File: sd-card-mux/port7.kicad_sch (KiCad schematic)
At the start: 10 parts, among them J201 47309-2285, U201 74LVC1G3157, U202 74LVC1G3157, U203 74LVC1G3157, U204 74LVC1G3157, U205 74LVC1G3157, U206 74LVC1G3157

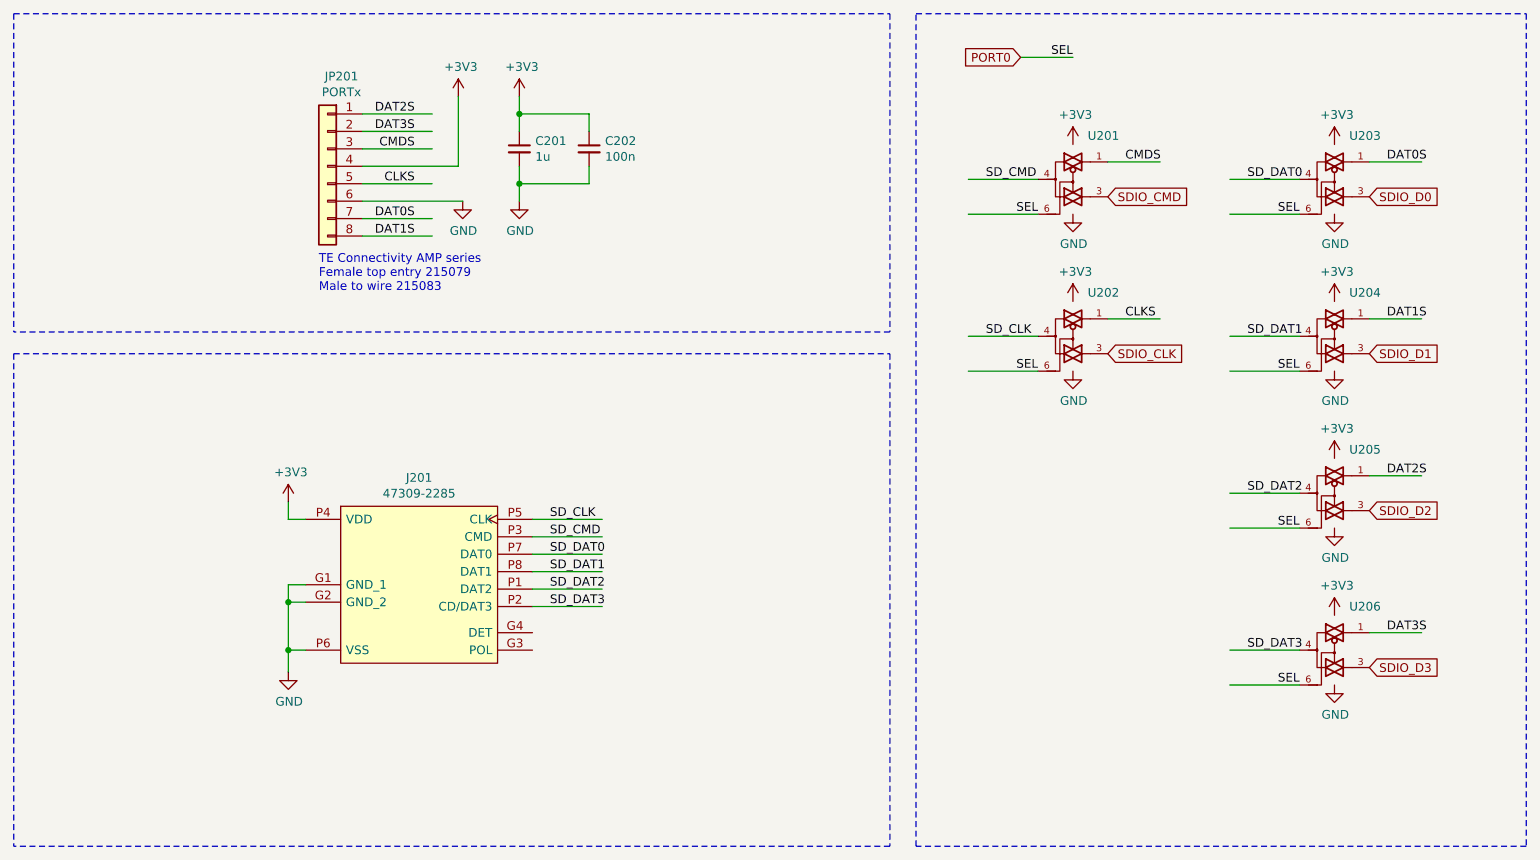
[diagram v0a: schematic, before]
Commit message: Added MCP23008 alternative
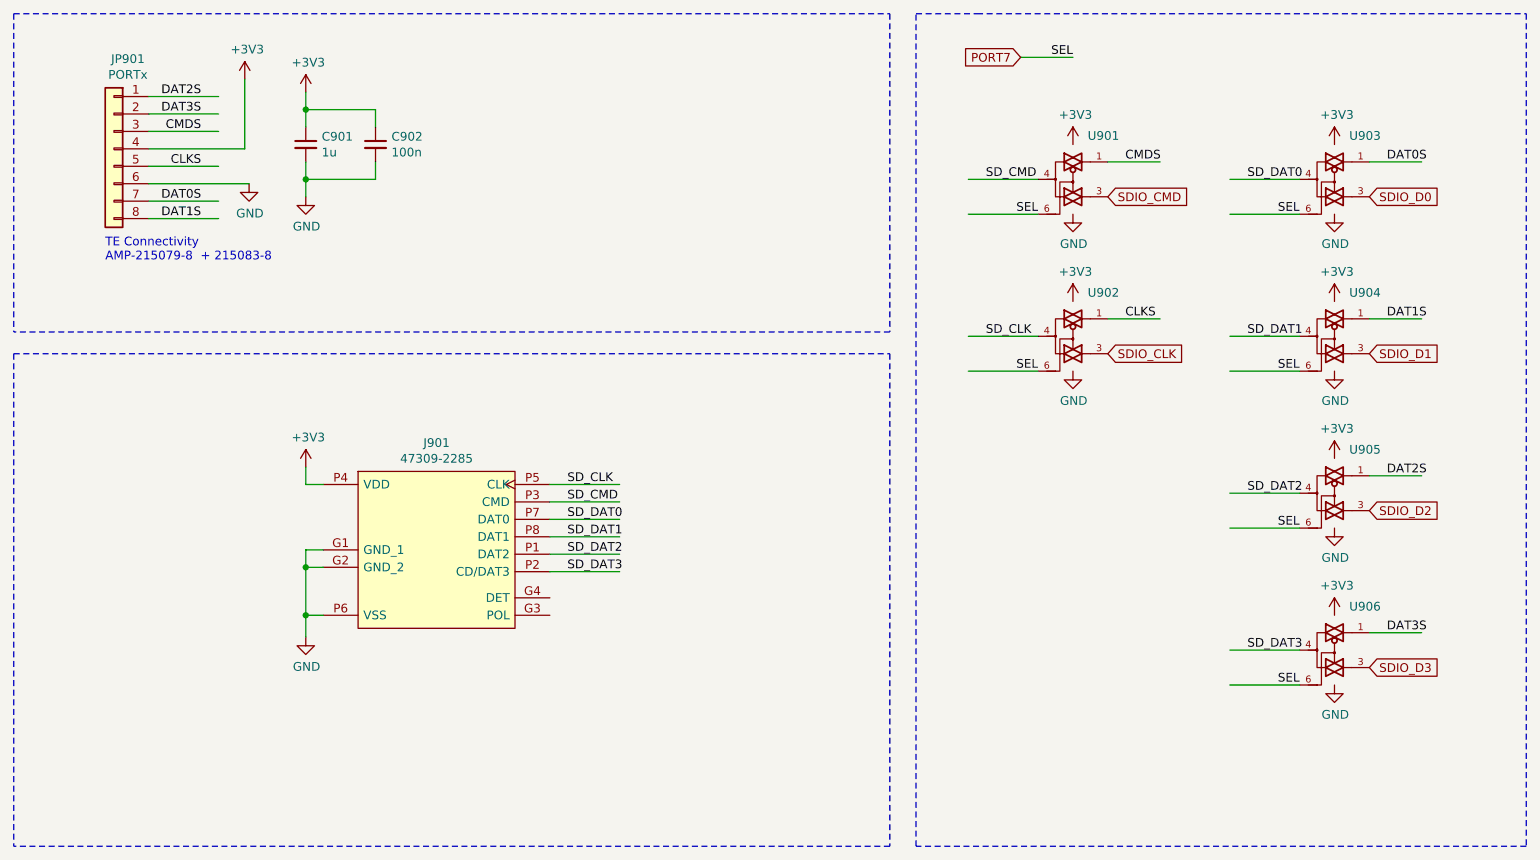
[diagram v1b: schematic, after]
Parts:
- removed C201: 1u, Capacitor_SMD:C_0402_1005Metric, symbol Device:C_Small
- removed C202: 100n, Capacitor_SMD:C_0402_1005Metric, symbol Device:C_Small
- removed J201: 47309-2285, footprints:47309-2285, symbol 47309-2285:47309-2285
- removed JP201: PORTx, Connector_JST:JST_PH_S8B-PH-K_1x08_P2.00mm_Horizontal, symbol Connector_Generic:Conn_01x08
- removed U201, U202, U203, U204, U205, U206: 74LVC1G3157, Package_TO_SOT_SMD:SOT-363_SC-70-6, symbol 74LVC1G3157:74LVC1G3157
- added C901: 1u, Capacitor_SMD:C_0402_1005Metric, symbol Device:C_Small
- added C902: 100n, Capacitor_SMD:C_0402_1005Metric, symbol Device:C_Small
- added J901: 47309-2285, footprints:47309-2285, symbol 47309-2285:47309-2285
- added JP901: PORTx, Connector_JST:JST_PH_S8B-PH-K_1x08_P2.00mm_Horizontal, symbol Connector_Generic:Conn_01x08
- added U901, U902, U903, U904, U905, U906: 74LVC1G3157, Package_TO_SOT_SMD:SOT-363_SC-70-6, symbol 74LVC1G3157:74LVC1G3157
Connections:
- net +3V3: now also C901.1, C902.1, J901.P4 (VDD), JP901.4 (Pin_4), U901.5 (VCC), U902.5 (VCC), U903.5 (VCC), U904.5 (VCC), U905.5 (VCC), U906.5 (VCC)
- net CLKS: now also JP901.5 (Pin_5), U902.1
- net CMDS: now also JP901.3 (Pin_3), U901.1
- net DAT0S: now also JP901.7 (Pin_7), U903.1
- net DAT1S: now also JP901.8 (Pin_8), U904.1
- net DAT2S: now also JP901.1 (Pin_1), U905.1
- net DAT3S: now also JP901.2 (Pin_2), U906.1
- net GND: now also C901.2, C902.2, J901.G1 (GND_1), J901.G2 (GND_2), J901.P6 (VSS), JP901.6 (Pin_6), U901.2 (GND), U902.2 (GND), U903.2 (GND), U904.2 (GND), U905.2 (GND), U906.2 (GND)
- net SDIO_CLK: now also U902.3
- net SDIO_CMD: now also U901.3
- net SDIO_D0: now also U903.3
- net SDIO_D1: now also U904.3
- net SDIO_D2: now also U905.3
- net SDIO_D3: now also U906.3
- net SD_CLK: now also J901.P5 (CLK), U902.4
- net SD_CMD: now also J901.P3 (CMD), U901.4
- net SD_DAT0: now also J901.P7 (DAT0), U903.4
- net SD_DAT1: now also J901.P8 (DAT1), U904.4
- net SD_DAT2: now also J901.P1 (DAT2), U905.4
- net SD_DAT3: now also J901.P2 (CD/DAT3), U906.4
- new net PORT7: U901.6, U902.6, U903.6, U904.6, U905.6, U906.6
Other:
- note added: "TE Connectivity AMP-215079-8 + 215083-8"
- note removed: "TE Connectivity AMP series Female top entry 215079 Male to wire 215083"

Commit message: Addedd missing upload port
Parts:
- C901: LCSC Part# (none) -> C52923
- C902: LCSC Part# (none) -> C1525
- JP901: footprint Connector_JST:JST_PH_S8B-PH-K_1x08_P2.00mm_Horizontal -> footprints:ConnectorMicromatch-8
- U901, U902, U903, U904, U905, U906: LCSC Part# (none) -> C38663
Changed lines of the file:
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@@
 (kicad_sch (version 20200608) (host eeschema "(5.99.0-1973-g8c57821e9)")
-  (page 1 9)
+  (page 9 9)
   (paper "A4")
   (junction (at 63.5 33.02))
@@
       (effects (font (size 1.27 1.27)) hide)
     )
+    (property "LCSC Part#" "C52923" (id 4) (at 63.5 38.1 0)
+      (effects (font (size 1.27 1.27)) hide)
+    )
   )
   (symbol (lib_name "Device:C_Small_2") (lib_id "Device:C_Small") (at 73.66 38.1 0) (unit 1)
@@
       (effects (font (size 1.27 1.27)) hide)
     )
+    (property "LCSC Part#" "C1525" (id 4) (at 73.66 38.1 0)
+      (effects (font (size 1.27 1.27)) hide)
+    )
   )
   (symbol (lib_name "74LVC1G3157:74LVC1G3157_2") (lib_id "74LVC1G3157:74LVC1G3157") (at 175.26 43.18 0) (unit 1)
@@
       (effects (font (size 1.27 1.27)) hide)
     )
+    (property "LCSC Part#" " C38663" (id 4) (at 175.26 43.18 0)
+      (effects (font (size 1.27 1.27)) hide)
+    )
   )
   (symbol (lib_id "74LVC1G3157:74LVC1G3157") (at 175.26 66.04 0) (unit 1)
@@
       (effects (font (size 1.27 1.27)) hide)
     )
+    (property "LCSC Part#" " C38663" (id 4) (at 175.26 66.04 0)
+      (effects (font (size 1.27 1.27)) hide)
+    )
   )
   (symbol (lib_id "74LVC1G3157:74LVC1G3157") (at 213.36 43.18 0) (unit 1)
@@
       (effects (font (size 1.27 1.27)) hide)
     )
+    (property "LCSC Part#" " C38663" (id 4) (at 213.36 43.18 0)
+      (effects (font (size 1.27 1.27)) hide)
+    )
   )
   (symbol (lib_id "74LVC1G3157:74LVC1G3157") (at 213.36 66.04 0) (unit 1)
@@
       (effects (font (size 1.27 1.27)) hide)
     )
+    (property "LCSC Part#" " C38663" (id 4) (at 213.36 66.04 0)
+      (effects (font (size 1.27 1.27)) hide)
+    )
   )
   (symbol (lib_id "74LVC1G3157:74LVC1G3157") (at 213.36 88.9 0) (unit 1)
@@
       (effects (font (size 1.27 1.27)) hide)
     )
+    (property "LCSC Part#" " C38663" (id 4) (at 213.36 88.9 0)
+      (effects (font (size 1.27 1.27)) hide)
+    )
   )
   (symbol (lib_id "74LVC1G3157:74LVC1G3157") (at 213.36 111.76 0) (unit 1)
@@
       (effects (font (size 1.27 1.27)) hide)
     )
+    (property "LCSC Part#" " C38663" (id 4) (at 213.36 111.76 0)
+      (effects (font (size 1.27 1.27)) hide)
+    )
   )
   (symbol (lib_id "Connector_Generic:Conn_01x08") (at 35.56 38.735 0) (mirror y) (unit 1)
@@
     (property "Reference" "JP901" (id 0) (at 37.592 25.635 0))
     (property "Value" "PORTx" (id 1) (at 37.592 27.9335 0))
-    (property "Footprint" "Connector_JST:JST_PH_S8B-PH-K_1x08_P2.00mm_Horizontal" (id 2) (at 35.56 38.735 0)
-      (effects (font (size 1.27 1.27)) hide)
-    )
+    (property "Footprint" "footprints:ConnectorMicromatch-8" (id 2) (at 35.56 38.735 0)
+      (effects (font (size 1.27 1.27)) hide)
+    )

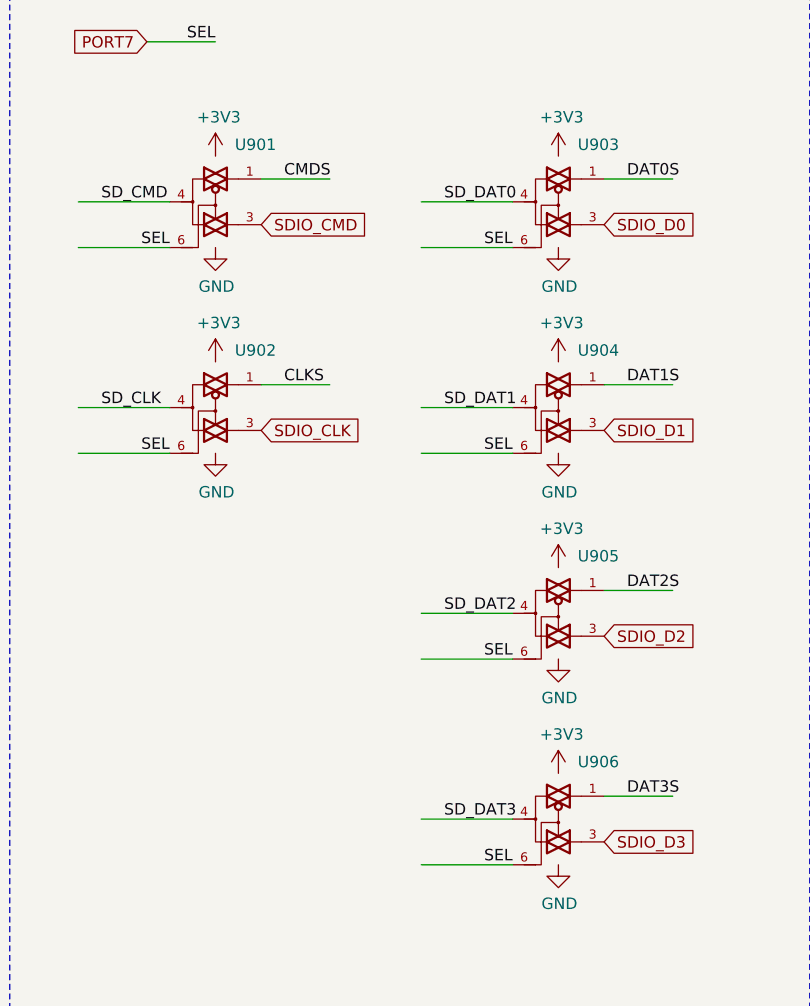
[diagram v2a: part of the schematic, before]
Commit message: Correction of inverted pins
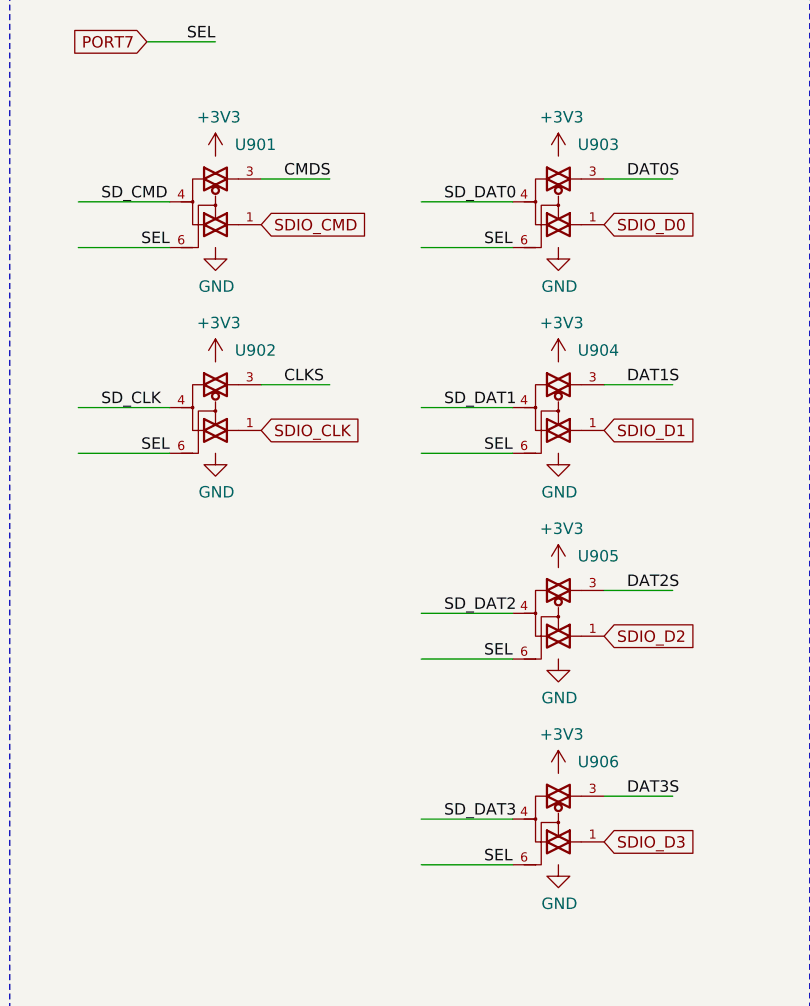
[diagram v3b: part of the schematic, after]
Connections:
- net CLKS: now also U902.3; no longer U902.1
- net CMDS: now also U901.3; no longer U901.1
- net DAT0S: now also U903.3; no longer U903.1
- net DAT1S: now also U904.3; no longer U904.1
- net DAT2S: now also U905.3; no longer U905.1
- net DAT3S: now also U906.3; no longer U906.1
- net SDIO_CLK: now also U902.1; no longer U902.3
- net SDIO_CMD: now also U901.1; no longer U901.3
- net SDIO_D0: now also U903.1; no longer U903.3
- net SDIO_D1: now also U904.1; no longer U904.3
- net SDIO_D2: now also U905.1; no longer U905.3
- net SDIO_D3: now also U906.1; no longer U906.3
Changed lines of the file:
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@@
     )
   )
-  (symbol (lib_id "74LVC1G3157:74LVC1G3157") (at 213.36 43.18 0) (unit 1)
+  (symbol (lib_name "74LVC1G3157:74LVC1G3157_5") (lib_id "74LVC1G3157:74LVC1G3157") (at 213.36 43.18 0) (unit 1)
     (in_bom yes) (on_board yes)
     (property "Reference" "U903" (id 0) (at 217.805 36.83 0))
@@
     )
   )
-  (symbol (lib_id "74LVC1G3157:74LVC1G3157") (at 213.36 66.04 0) (unit 1)
+  (symbol (lib_name "74LVC1G3157:74LVC1G3157_4") (lib_id "74LVC1G3157:74LVC1G3157") (at 213.36 66.04 0) (unit 1)
     (in_bom yes) (on_board yes)
     (property "Reference" "U904" (id 0) (at 217.805 59.69 0))
@@
     )
   )
-  (symbol (lib_id "74LVC1G3157:74LVC1G3157") (at 213.36 88.9 0) (unit 1)
+  (symbol (lib_name "74LVC1G3157:74LVC1G3157_3") (lib_id "74LVC1G3157:74LVC1G3157") (at 213.36 88.9 0) (unit 1)
     (in_bom yes) (on_board yes)
     (property "Reference" "U905" (id 0) (at 217.805 82.55 0))
@@
     )
   )
-  (symbol (lib_id "74LVC1G3157:74LVC1G3157") (at 213.36 111.76 0) (unit 1)
+  (symbol (lib_name "74LVC1G3157:74LVC1G3157_1") (lib_id "74LVC1G3157:74LVC1G3157") (at 213.36 111.76 0) (unit 1)
     (in_bom yes) (on_board yes)
     (property "Reference" "U906" (id 0) (at 217.805 105.41 0))

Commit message: Removal of host port and preparation for manufacturing
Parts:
- J901: Mechanical (none) -> T
- JP901: Mechanical (none) -> T; TME Part# (none) -> MM2x5
- U901, U902, U903, U904, U905, U906: LCSC Part# C38663 -> C265126; Rotation (none) -> 0
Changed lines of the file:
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@@
       (effects (font (size 1.27 1.27)) hide)
     )
-    (property "LCSC Part#" " C38663" (id 4) (at 175.26 43.18 0)
+    (property "LCSC Part#" "C265126" (id 4) (at 175.26 43.18 0)
+      (effects (font (size 1.27 1.27)) hide)
+    )
+    (property "Rotation" "0" (id 4) (at 175.26 43.18 0)
       (effects (font (size 1.27 1.27)) hide)
     )
@@
       (effects (font (size 1.27 1.27)) hide)
     )
-    (property "LCSC Part#" " C38663" (id 4) (at 175.26 66.04 0)
+    (property "LCSC Part#" "C265126" (id 4) (at 175.26 66.04 0)
+      (effects (font (size 1.27 1.27)) hide)
+    )
+    (property "Rotation" "0" (id 4) (at 175.26 66.04 0)
       (effects (font (size 1.27 1.27)) hide)
     )
@@
       (effects (font (size 1.27 1.27)) hide)
     )
-    (property "LCSC Part#" " C38663" (id 4) (at 213.36 43.18 0)
+    (property "LCSC Part#" "C265126" (id 4) (at 213.36 43.18 0)
+      (effects (font (size 1.27 1.27)) hide)
+    )
+    (property "Rotation" "0" (id 4) (at 213.36 43.18 0)
       (effects (font (size 1.27 1.27)) hide)
     )
@@
       (effects (font (size 1.27 1.27)) hide)
     )
-    (property "LCSC Part#" " C38663" (id 4) (at 213.36 66.04 0)
+    (property "LCSC Part#" "C265126" (id 4) (at 213.36 66.04 0)
+      (effects (font (size 1.27 1.27)) hide)
+    )
+    (property "Rotation" "0" (id 4) (at 213.36 66.04 0)
       (effects (font (size 1.27 1.27)) hide)
     )
@@
       (effects (font (size 1.27 1.27)) hide)
     )
-    (property "LCSC Part#" " C38663" (id 4) (at 213.36 88.9 0)
+    (property "LCSC Part#" "C265126" (id 4) (at 213.36 88.9 0)
+      (effects (font (size 1.27 1.27)) hide)
+    )
+    (property "Rotation" "0" (id 4) (at 213.36 88.9 0)
       (effects (font (size 1.27 1.27)) hide)
     )
@@
       (effects (font (size 1.27 1.27)) hide)
     )
-    (property "LCSC Part#" " C38663" (id 4) (at 213.36 111.76 0)
+    (property "LCSC Part#" "C265126" (id 4) (at 213.36 111.76 0)
+      (effects (font (size 1.27 1.27)) hide)
+    )
+    (property "Rotation" "0" (id 4) (at 213.36 111.76 0)
       (effects (font (size 1.27 1.27)) hide)
     )
@@
     )
     (property "Datasheet" "~" (id 3) (at 35.56 38.735 0)
+      (effects (font (size 1.27 1.27)) hide)
+    )
+    (property "TME Part#" "MM2x5" (id 4) (at 35.56 38.735 0)
+      (effects (font (size 1.27 1.27)) hide)
+    )
+    (property "Mechanical" "T" (id 4) (at 35.56 38.735 0)
       (effects (font (size 1.27 1.27)) hide)
     )
@@
       (effects (font (size 1.27 1.27)) (justify left) hide)
     )
+    (property "Mechanical" "T" (id 4) (at 66.04 88.265 0)
+      (effects (font (size 1.27 1.27)) hide)
+    )
   )
